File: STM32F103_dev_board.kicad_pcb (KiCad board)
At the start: 4 copper layers, 39.4 x 83.8 mm, 39 parts, among them IC1 TLV70233DBVR, IC2 FT232RNL-REEL, J1 Conn_ARM_JTAG_SWD_20, J2 Conn_01x20_Pin, J3 Conn_01x20_Pin, J4 Conn_02x03_Odd_Even, J6 USB4800-03-A, U1 STM32F103RBTx, Y1 8MHz, Y2 Crystal_GND23

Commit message: changed LDO to TLV75733PDBVR
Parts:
- removed IC1: TLV70233DBVR, SamacSys_Parts:SOT95P280X145-5N
- added PS1: TLV75733PDBVR, SamacSys_Parts:SOT95P280X145-5N, F.Cu at (153.4, 126.1)
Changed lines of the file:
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@@
   (title_block
     (title "STM32F103RBT6 Dev Board")
-    (date "2023-10-13")
-    (rev "1.1.2")
+    (date "2023-11-17")
+    (rev "1.1.3")
   )
   (layers
@@
   (net 70 "unconnected-(IC2-CBUS3-Pad14)")
   (net 71 "unconnected-(IC2-CBUS1-Pad22)")
-  (net 72 "unconnected-(IC1-NC-Pad4)")
+  (net 72 "unconnected-(PS1-NC-Pad4)")
   (net 73 "unconnected-(IC2-CBUS0-Pad23)")
   (net 74 "unconnected-(IC2-NC_2-Pad24)")
@@
     )
   )
+  (footprint "SamacSys_Parts:SOT95P280X145-5N" (layer "F.Cu")
+    (at 153.355 126.091 90)
+    (descr "SOT23")
+    (tags "Power Supply")
+    (property "Arrow Part Number" "TLV75733PDBVR")
+    (property "Arrow Price/Stock" "https://www.arrow.com/en/products/tlv75733pdbvr/texas-instruments?region=nac")
+    (property "Height" "1.45")
+    (property "Manufacturer_Name" "Texas Instruments")
+    (property "Manufacturer_Part_Number" "TLV75733PDBVR")
+    (property "Mouser Part Number" "595-TLV75733PDBVR")
+    (property "Mouser Price/Stock" "https://www.mouser.co.uk/ProductDetail/Texas-Instruments/TLV75733PDBVR?qs=y6ZabgHbY%252BwAAzSntTW34w%3D%3D")
+    (property "Sheetfile" "STM32F103_dev_board.kicad_sch")
+    (property "Sheetname" "")
+    (property "ki_description" "LDO Voltage Regulators 1A Low-IQ Small-Size Low-Dropout (LDO) Regulator 5-SOT-23 -40 to 125")
+    (attr smd)
+    (fp_text reference "PS1" (at 0 2.855 90) (layer "F.SilkS")
+        (effects (font (size 1.27 1.27) (thickness 0.254)))
+    )
+    (fp_text value "TLV75733PDBVR" (at 0 0 90) (layer "F.SilkS") hide
+        (effects (font (size 1.27 1.27) (thickness 0.254)))
+    )
+    (fp_text user "${REFERENCE}" (at 0 0 90) (layer "F.Fab")
+        (effects (font (size 1.27 1.27) (thickness 0.254)))
+    )
+    (fp_line (start -1.85 -1.5) (end -0.65 -1.5)
+      (stroke (width 0.2) (type solid)) (layer "F.SilkS"))
+    (fp_line (start -0.3 -1.45) (end 0.3 -1.45)
+      (stroke (width 0.2) (type solid)) (layer "F.SilkS"))
+    (fp_line (start -0.3 1.45) (end -0.3 -1.45)
+      (stroke (width 0.2) (type solid)) (layer "F.SilkS"))
+    (fp_line (start 0.3 -1.45) (end 0.3 1.45)
+      (stroke (width 0.2) (type solid)) (layer "F.SilkS"))
+    (fp_line (start 0.3 1.45) (end -0.3 1.45)
+      (stroke (width 0.2) (type solid)) (layer "F.SilkS"))
+    (fp_line (start -2.1 -1.775) (end 2.1 -1.775)
+      (stroke (width 0.05) (type solid)) (layer "F.CrtYd"))
+    (fp_line (start -2.1 1.775) (end -2.1 -1.775)
+      (stroke (width 0.05) (type solid)) (layer "F.CrtYd"))
+    (fp_line (start 2.1 -1.775) (end 2.1 1.775)
+      (stroke (width 0.05) (type solid)) (layer "F.CrtYd"))
+    (fp_line (start 2.1 1.775) (end -2.1 1.775)
+      (stroke (width 0.05) (type solid)) (layer "F.CrtYd"))
+    (fp_line (start -0.8 -1.45) (end 0.8 -1.45)
+      (stroke (width 0.1) (type solid)) (layer "F.Fab"))
+    (fp_line (start -0.8 -0.5) (end 0.15 -1.45)
+      (stroke (width 0.1) (type solid)) (layer "F.Fab"))
+    (fp_line (start -0.8 1.45) (end -0.8 -1.45)
+      (stroke (width 0.1) (type solid)) (layer "F.Fab"))
+    (fp_line (start 0.8 -1.45) (end 0.8 1.45)
+      (stroke (width 0.1) (type solid)) (layer "F.Fab"))
+    (fp_line (start 0.8 1.45) (end -0.8 1.45)
+      (stroke (width 0.1) (type solid)) (layer "F.Fab"))
+    (pad "1" smd rect (at -1.25 -0.95 180) (size 0.6 1.2) (layers "F.Cu" "F.Paste" "F.Mask")
+      (net 80 "5V") (pinfunction "IN") (pintype "power_in"))
+    (pad "2" smd rect (at -1.25 0 180) (size 0.6 1.2) (layers "F.Cu" "F.Paste" "F.Mask")
+      (net 79 "GND") (pinfunction "GND") (pintype "power_in"))
+    (pad "3" smd rect (at -1.25 0.95 180) (size 0.6 1.2) (layers "F.Cu" "F.Paste" "F.Mask")
+      (net 80 "5V") (pinfunction "EN") (pintype "input"))
+    (pad "4" smd rect (at 1.25 0.95 180) (size 0.6 1.2) (layers "F.Cu" "F.Paste" "F.Mask")
+      (net 72 "unconnected-(PS1-NC-Pad4)") (pinfunction "NC") (pintype "no_connect"))
+    (pad "5" smd rect (at 1.25 -0.95 180) (size 0.6 1.2) (layers "F.Cu" "F.Paste" "F.Mask")
+      (net 81 "VCC3V3") (pinfunction "OUT") (pintype "output"))
+    (model "C:\\lib\\samacsys\\SamacSys_Parts.3dshapes\\TLV75733PDBVR.stp"
+      (offset (xyz 0 0 0))
+      (scale (xyz 1 1 1))
+      (rotate (xyz 0 0 0))
+    )
+  )
   (footprint "Connector_PinHeader_2.54mm:PinHeader_2x03_P2.54mm_Vertical" (layer "F.Cu")
     (at 137.155 123.785)
@@
     )
   )
-  (footprint "SamacSys_Parts:SOT95P280X145-5N" (layer "F.Cu")
-    (at 153.355 126.091 90)
-    (descr "DBV0005A")
-    (tags "Integrated Circuit")
-    (property "Height" "1.45")
-    (property "Manufacturer_Name" "Texas Instruments")
-    (property "Manufacturer_Part_Number" "TLV70233DBVR")
-    (property "Mouser Part Number" "595-TLV70233DBVR")
-    (property "Mouser Price/Stock" "https://www.mouser.co.uk/ProductDetail/Texas-Instruments/TLV70233DBVR?qs=zQ2yIHQ6k3wiHrD0NUI05Q%3D%3D")
-    (property "Sheetfile" "STM32F103_dev_board.kicad_sch")
-    (property "Sheetname" "")
-    (property "ki_description" "300mA Low-Iq Low-Dropout (LDO) Regulator for Portables")
-    (attr smd)
-    (fp_text reference "IC1" (at -0.02 2.601 90) (layer "F.SilkS")
-        (effects (font (size 1.27 1.27) (thickness 0.254)))
-    )
-    (fp_text value "TLV70233DBVR" (at 0 0 90) (layer "F.SilkS") hide
-        (effects (font (size 1.27 1.27) (thickness 0.254)))
-    )
-    (fp_text user "${REFERENCE}" (at 0 0 90) (layer "F.Fab")
-        (effects (font (size 1.27 1.27) (thickness 0.254)))
-    )
-    (fp_line (start -1.85 -1.5) (end -0.65 -1.5)
-      (stroke (width 0.2) (type solid)) (layer "F.SilkS"))
-    (fp_line (start -0.3 -1.45) (end 0.3 -1.45)
-      (stroke (width 0.2) (type solid)) (layer "F.SilkS"))
-    (fp_line (start -0.3 1.45) (end -0.3 -1.45)
-      (stroke (width 0.2) (type solid)) (layer "F.SilkS"))
-    (fp_line (start 0.3 -1.45) (end 0.3 1.45)
-      (stroke (width 0.2) (type solid)) (layer "F.SilkS"))
-    (fp_line (start 0.3 1.45) (end -0.3 1.45)
-      (stroke (width 0.2) (type solid)) (layer "F.SilkS"))
-    (fp_line (start -2.1 -1.775) (end 2.1 -1.775)
-      (stroke (width 0.05) (type solid)) (layer "F.CrtYd"))
-    (fp_line (start -2.1 1.775) (end -2.1 -1.775)
-      (stroke (width 0.05) (type solid)) (layer "F.CrtYd"))
-    (fp_line (start 2.1 -1.775) (end 2.1 1.775)
-      (stroke (width 0.05) (type solid)) (layer "F.CrtYd"))
-    (fp_line (start 2.1 1.775) (end -2.1 1.775)
-      (stroke (width 0.05) (type solid)) (layer "F.CrtYd"))
-    (fp_line (start -0.8 -1.45) (end 0.8 -1.45)
-      (stroke (width 0.1) (type solid)) (layer "F.Fab"))
-    (fp_line (start -0.8 -0.5) (end 0.15 -1.45)
-      (stroke (width 0.1) (type solid)) (layer "F.Fab"))
-    (fp_line (start -0.8 1.45) (end -0.8 -1.45)
-      (stroke (width 0.1) (type solid)) (layer "F.Fab"))
-    (fp_line (start 0.8 -1.45) (end 0.8 1.45)
-      (stroke (width 0.1) (type solid)) (layer "F.Fab"))
-    (fp_line (start 0.8 1.45) (end -0.8 1.45)
-      (stroke (width 0.1) (type solid)) (layer "F.Fab"))
-    (pad "1" smd rect (at -1.25 -0.95 180) (size 0.6 1.2) (layers "F.Cu" "F.Paste" "F.Mask")
-      (net 80 "5V") (pinfunction "IN") (pintype "passive"))
-    (pad "2" smd rect (at -1.25 0 180) (size 0.6 1.2) (layers "F.Cu" "F.Paste" "F.Mask")
-      (net 79 "GND") (pinfunction "GND") (pintype "passive"))
-    (pad "3" smd rect (at -1.25 0.95 180) (size 0.6 1.2) (layers "F.Cu" "F.Paste" "F.Mask")
-      (net 80 "5V") (pinfunction "EN") (pintype "passive"))
-    (pad "4" smd rect (at 1.25 0.95 180) (size 0.6 1.2) (layers "F.Cu" "F.Paste" "F.Mask")
-      (net 72 "unconnected-(IC1-NC-Pad4)") (pinfunction "NC") (pintype "no_connect"))
-    (pad "5" smd rect (at 1.25 -0.95 180) (size 0.6 1.2) (layers "F.Cu" "F.Paste" "F.Mask")
-      (net 81 "VCC3V3") (pinfunction "OUT") (pintype "passive"))
-    (model "C:\\lib\\KiCad_Library\\SamacSys_Parts.3dshapes\\TLV70233DBVR.stp"
-      (offset (xyz 0 0 0))
-      (scale (xyz 1 1 1))
-      (rotate (xyz 0 0 0))
-    )
-  )
   (footprint "Resistor_SMD:R_0603_1608Metric_Pad0.98x0.95mm_HandSolder" (layer "F.Cu")
     (at 153.67 78.395 -90)
@@
     (pad "28" smd rect (at 3.512 4.225 180) (size 0.45 1.725) (layers "B.Cu" "B.Paste" "B.Mask")
       (net 77 "unconnected-(IC2-OSCO-Pad28)") (pinfunction "OSCO") (pintype "passive+no_connect"))
-    (model "C:\\lib\\KiCad_Library\\SamacSys_Parts.3dshapes\\FT232RNL-REEL.stp"
+    (model "C:\\lib\\samacsys\\SamacSys_Parts.3dshapes\\FT232RNL-REEL.stp"
       (offset (xyz 0 0 0))
       (scale (xyz 1 1 1))
@@
   (segment (start 143.51 113.030685) (end 143.51 114.88) (width 0.25) (layer "F.Cu") (net 81))
   (segment (start 142.484695 114.88) (end 141.444695 115.92) (width 0.25) (layer "F.Cu") (net 81))
-  (segment (start 152.34 125.1) (end 152.4 125.04) (width 0.25) (layer "F.Cu") (net 81))
   (segment (start 149.205 119.345) (end 150.911 119.345) (width 0.25) (layer "F.Cu") (net 81))
   (segment (start 149.205 116.765) (end 148.59 116.15) (width 0.25) (layer "F.Cu") (net 81))

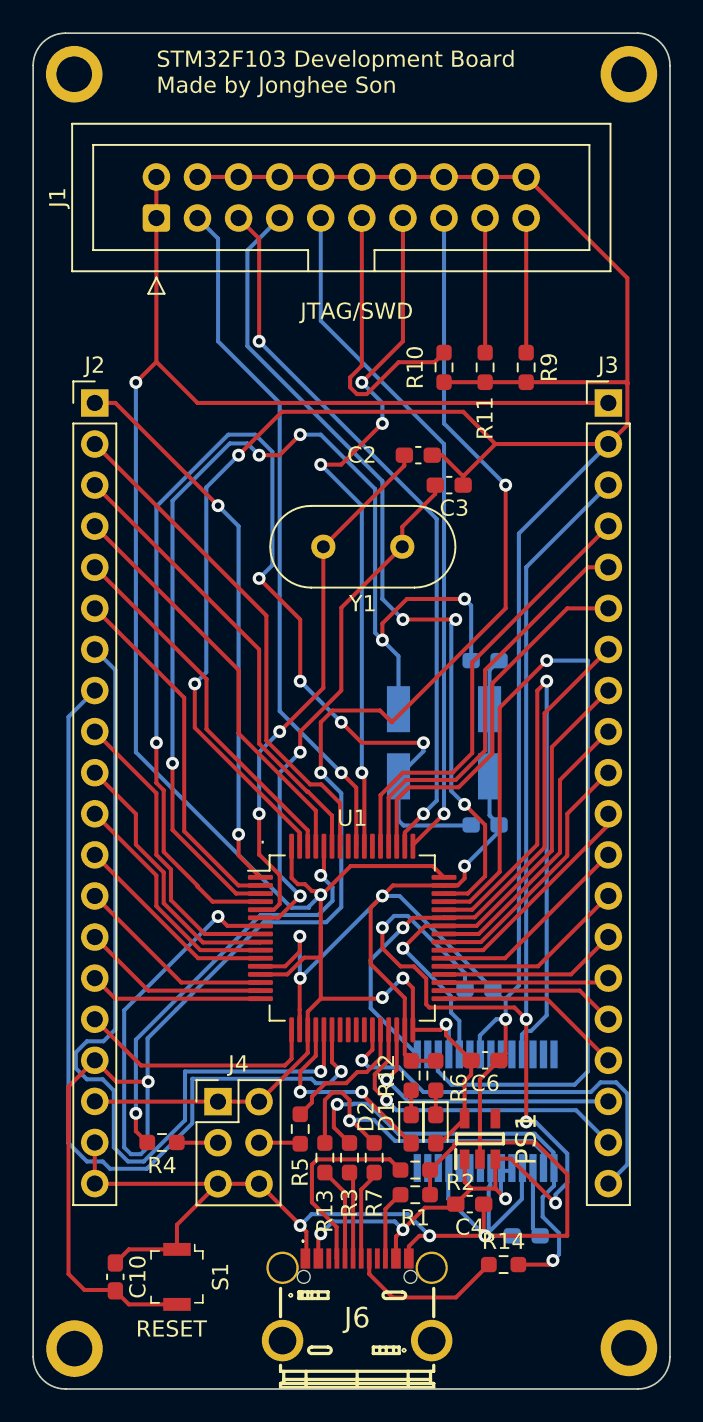
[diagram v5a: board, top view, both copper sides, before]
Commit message: Added silkscreen marking for gpio pins
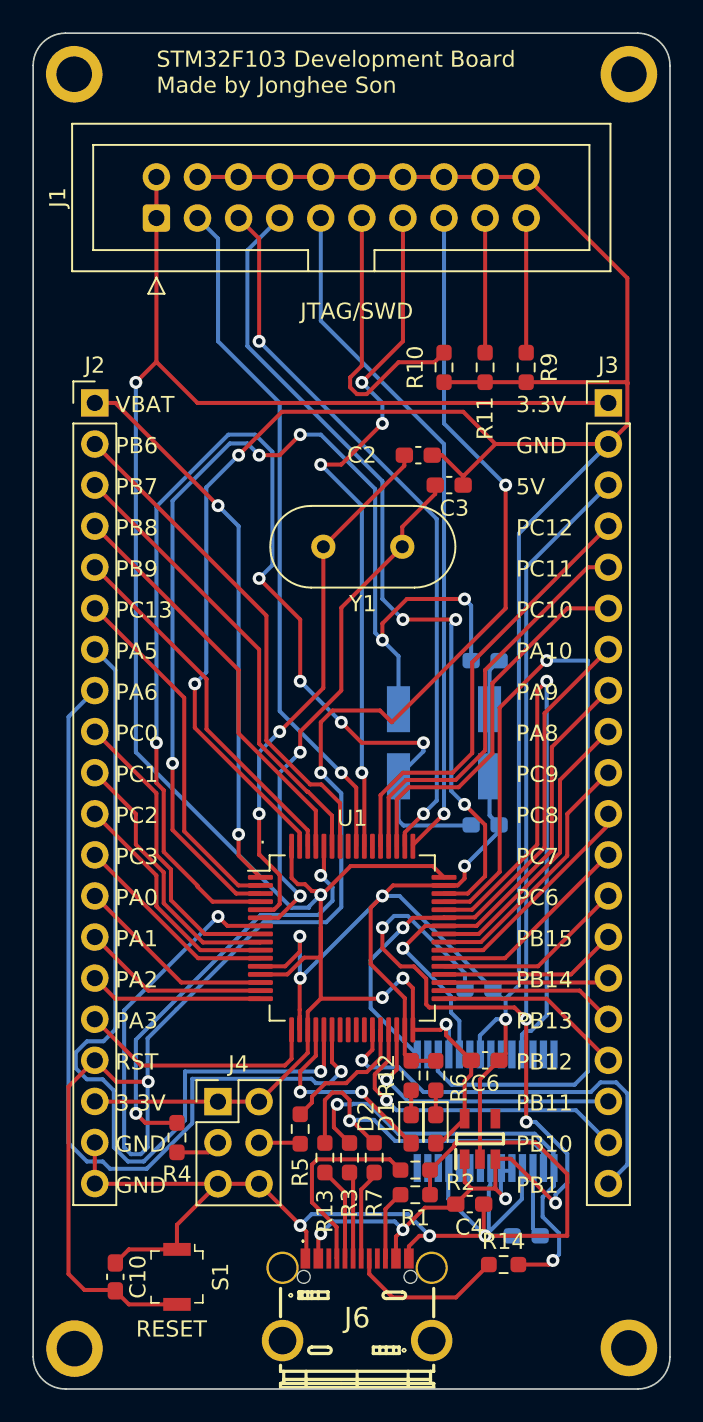
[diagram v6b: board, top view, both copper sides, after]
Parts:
- moved R4 0.97 mm to (134.6, 126.0), turned to 90 degrees
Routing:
- net BOOT0: track 26.1 -> 26.8 mm
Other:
- board text added: "3.3V"
- board text added: "5V"
- board text added: "GND"
- board text added: "PA0"
- board text added: "PA1"
- board text added: "PA10"
- board text added: "PA2"
- board text added: "PA3"
- board text added: "PA5"
- board text added: "PA6"
- board text added: "PA8"
- board text added: "PA9"
- board text added: "PB1"
- board text added: "PB10"
- board text added: "PB11"
- board text added: "PB12"
- board text added: "PB13"
- board text added: "PB14"
- board text added: "PB15"
- board text added: "PB6"
- board text added: "PB7"
- board text added: "PB8"
- board text added: "PB9"
- board text added: "PC0"
- board text added: "PC1"
- board text added: "PC10"
- board text added: "PC11"
- board text added: "PC12"
- board text added: "PC13"
- board text added: "PC2"
- board text added: "PC3"
- board text added: "PC6"
- board text added: "PC7"
- board text added: "PC8"
- board text added: "PC9"
- board text added: "RST"
- board text added: "VBAT"

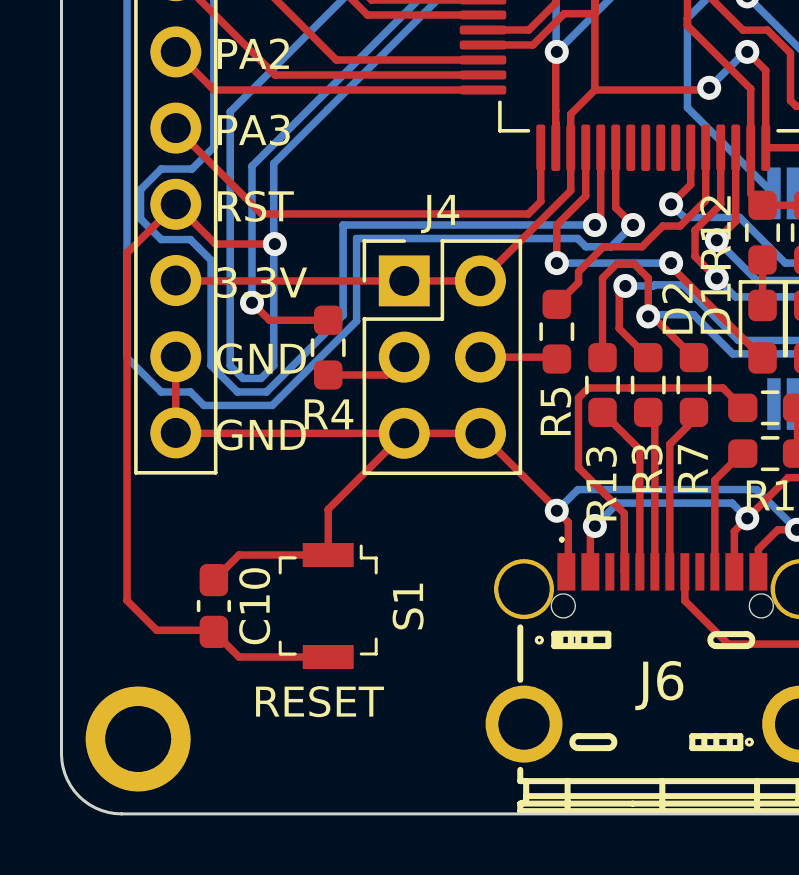
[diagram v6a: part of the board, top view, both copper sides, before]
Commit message: Changed boot mode selector to SPDT slide switch
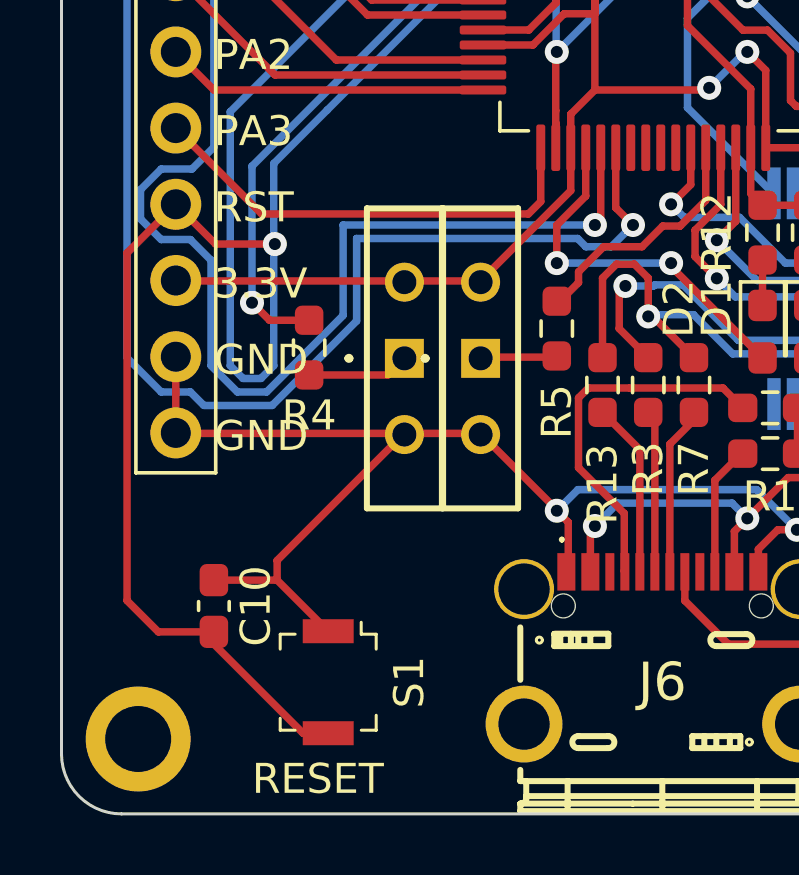
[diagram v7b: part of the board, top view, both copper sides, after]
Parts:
- removed J4: Conn_02x03_Odd_Even, Connector_PinHeader_2.54mm:PinHeader_2x03_P2.54mm_Vertical
- added S2: BSI-10, SamacSys_Parts:BSI10, F.Cu at (137.2, 126.4)
- added S3: BSI-10, SamacSys_Parts:BSI10, F.Cu at (139.7, 126.4)
- moved S1 2.54 mm to (134.6, 137.2)
- moved R4 0.63 mm to (134.0, 126.0)
- moved R5 0.10 mm to (142.2, 125.4)
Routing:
- net GND: track 304.3 -> 306.2 mm
- net RESET: track 121.2 -> 122.5 mm
- net BOOT0: track 26.8 -> 26.2 mm
- net Net-(S2-COM): track 2.78 -> 3.40 mm

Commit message: Changed my personal website URL on board silkscreen
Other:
- board text added: "https://jhson.dev"
- board text removed: "https://paperecord.com"
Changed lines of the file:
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@@
     (title "STM32F103RBT6 Dev Board")
     (date "2023-12-14")
-    (rev "1.2.0")
+    (rev "1.2.1")
   )
   (layers
@@
   (gr_line (start 127.73 57.73) (end 163.1 57.73)
     (stroke (width 0.1) (type default)) (layer "Edge.Cuts"))
-  (gr_text "https://paperecord.com" (at 154.94 59.69) (layer "B.SilkS")
+  (gr_text "https://jhson.dev" (at 151.765 59.69) (layer "B.SilkS")
     (effects (font (size 1 1) (thickness 0.15)) (justify left bottom mirror))
   )
